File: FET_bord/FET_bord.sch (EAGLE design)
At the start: 4 parts

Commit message: スナバ回路資料追加
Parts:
- added CPOL1, CPOL2, CPOL3: C_DEKAI, user_rcl:C_DEKAI
- added R1: 0, user_rcl:R_REG
- added R_I1, R_I2: (no value), user_rcl:R_SHUGOU
- added U$1: VL_4P, user_conector:VL_4P
- added U$2: A3921, user_ic:A3921
- added U$3: ACS711, user_ic:ACS711
- added U$4: HS38382, user_heatshink:HS38382
- added U$5, U$7: FDC6305, user_tr_fet_igbt:FDC6305
- added U$6: RGB_LED, user_leds:RGB_LED
- added U$8: TLP290-4, user_ic:TLP290-4
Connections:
- new net FF1: U$5.PIN1_G1, U$7.PIN1_G1
- new net FF2: U$5.PIN3_G2, U$7.PIN3_G2
- new net GHA: U$2.PIN10_GHA
- new net GHB: U$2.PIN5_GHB
- new net GLA: U$2.PIN12_GLA
- new net GLB: U$2.PIN3_GLB
- new net GND: CPOL1.-, CPOL2.-, CPOL3.-, R1.2, TR3.PIN3_S, TR4.PIN3_S, U$1.PIN4
- new net GNDI: R1.1, U$2.PAD, U$2.PIN17_GND, U$5.PIN2_S2, U$5.PIN5_S1, U$6.B_A
- new net M: U$1.PIN3, U$3.1_IP+, U$3.2_IP+
- new net N$1: U$5.PIN6_D1, U$6.R_A
- new net N$2: TR1.PIN3_S, TR3.PIN2_D, U$3.3_IP-, U$3.4_IP-
- new net N$3: TR2.PIN3_S, TR4.PIN2_D
- new net N$4: U$1.PIN2
- new net N$5: U$5.PIN4_D2, U$6.G_A
- new net N$6: R_I1.1, U$6.R_K
- new net N$7: R_I1.2, U$6.G_K
- new net N$8: R_I1.3, U$6.B_K
- new net SA: U$2.PIN11_SA
- new net SB: U$2.PIN4_SB
- new net VDD: CPOL1.+, CPOL2.+, CPOL3.+, TR1.PIN2_D, TR2.PIN2_D, U$1.PIN1

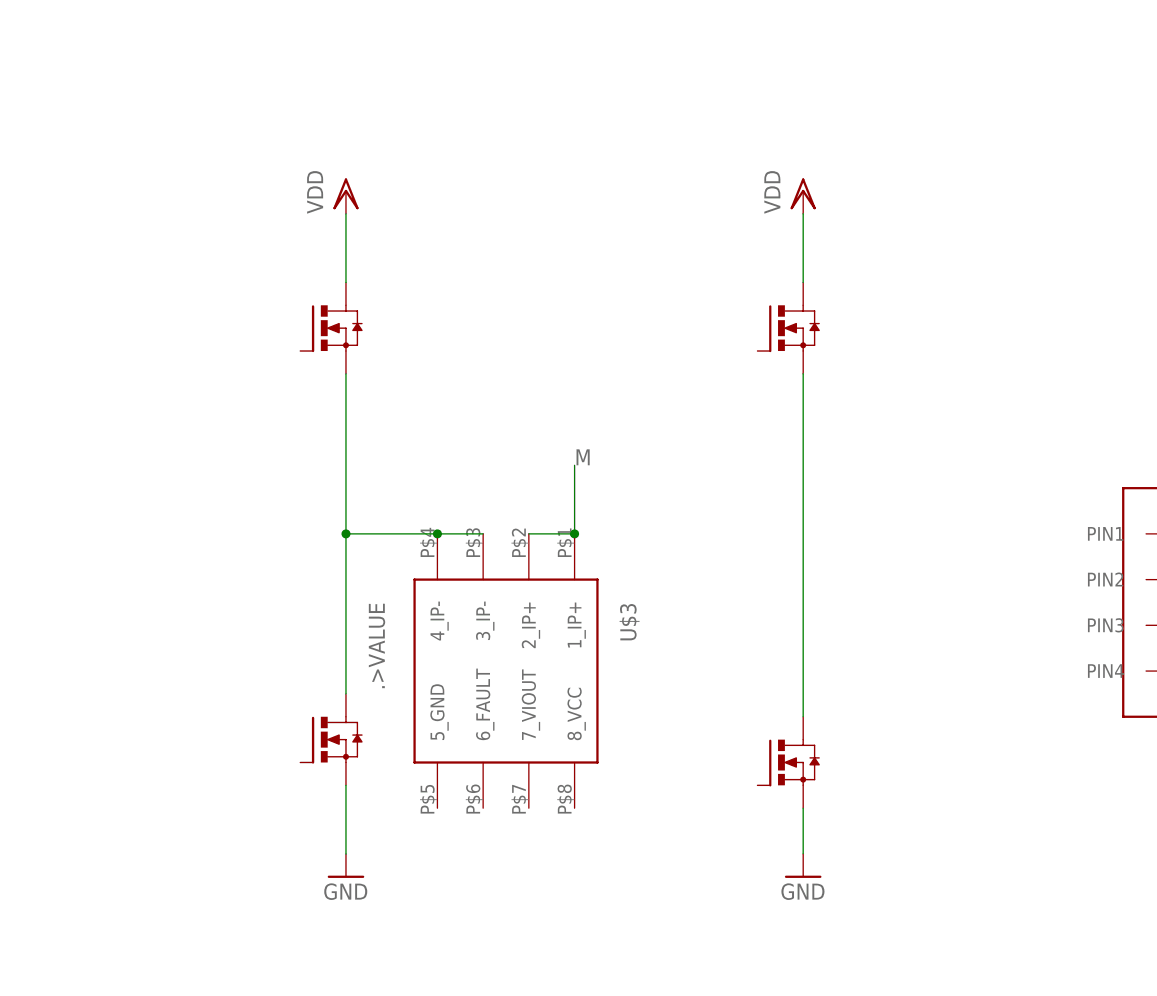
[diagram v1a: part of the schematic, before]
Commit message: スナバ追加
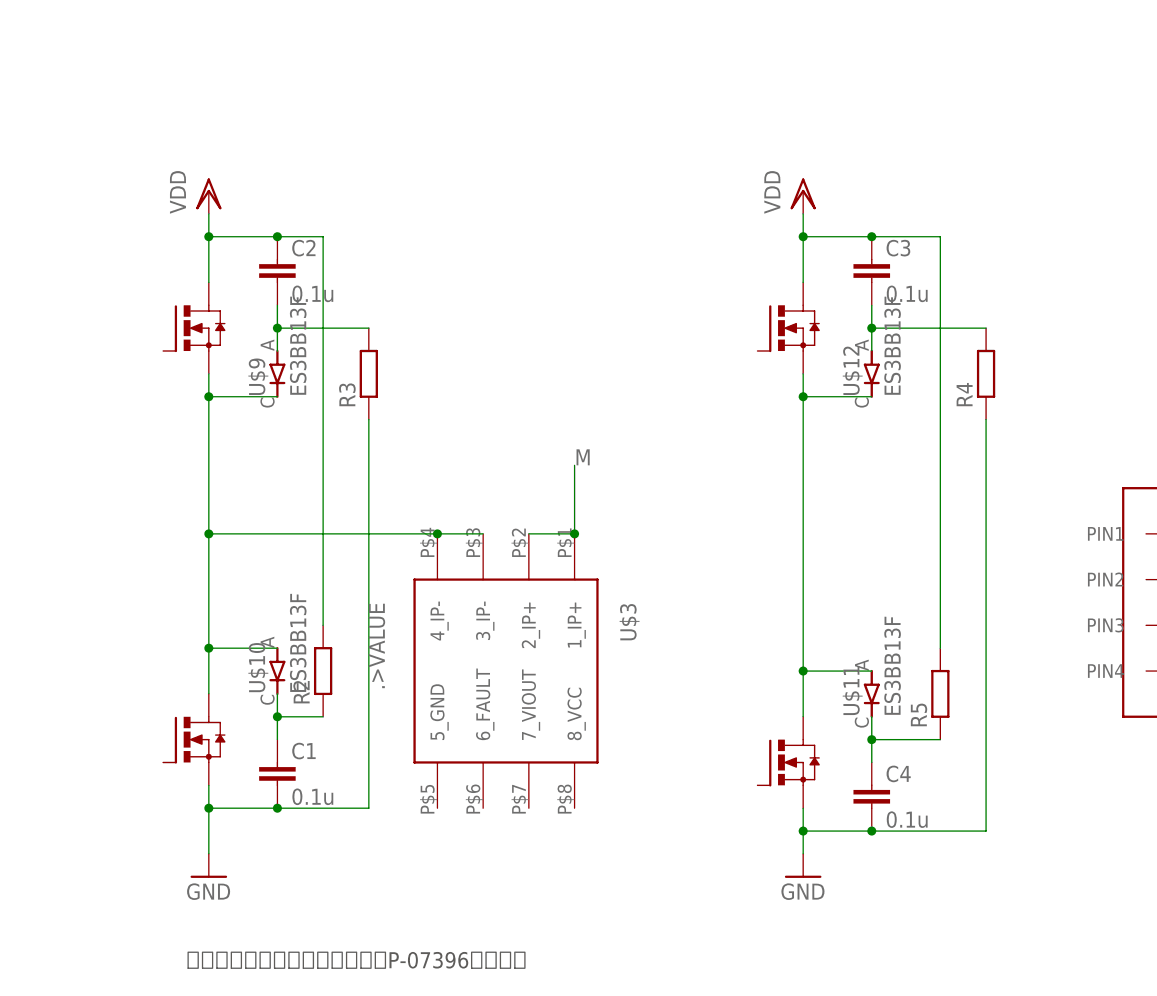
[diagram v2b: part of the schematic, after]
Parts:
- added C1, C2, C3, C4: 0.1u, rcl:C-EUC3216
- added R2, R3, R4, R5: (no value), user_rcl:R_REG1632*
- added U$10, U$11, U$12, U$9: ES3BB13F, user_diode:ES3BB13F
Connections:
- new net N$10: C2.2, R3.2, U$9.A
- new net N$11: C3.2, R4.2, U$12.A
- new net N$12: C4.1, R5.1, U$11.C
- new net N$9: C1.1, R2.1, U$10.C
- net GND: now also C1.2, C4.2, R3.1, R4.1
- net N$2: now also U$10.A, U$9.C
- net N$3: now also U$11.A, U$12.C
- net VDD: now also C2.1, C3.1, R2.2, R5.2
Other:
- note added: "スナバコンデンサは秋月電子のP-07396を用いる"

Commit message: a3921ロジック回路周りの設計
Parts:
- added C5: 0.1u, rcl:C-EUC1608
- added R6: (no value), user_rcl:R_REG
- added R7: 20k, user_rcl:R_REG
- added R_I3, R_I4: 10k, user_rcl:R_SHUGOU2
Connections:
- new net N$13: R_I3.1, U$2.PIN23_PWMH
- new net N$14: R_I3.2, U$2.PIN22_PWML
- new net N$15: R_I3.3, U$2.PIN21_SR
- new net N$16: R_I3.4, U$2.PIN19_PHASE
- new net RDEAD: U$2.PIN27_RDEAD
- new net RESET: U$2.PIN24_RESET
- new net V5: C5.1, R_I3.5, R_I3.6, R_I3.7, R_I4.5, R_I4.6, R_I4.7, U$2.PIN20_V5
- new net VDSTH: R6.1, R7.1, R_I4.1, R_I4.4, U$2.PIN28_VDSTH
- net FF1: now also R_I4.2, U$2.PIN25_FF1
- net FF2: now also R_I4.3, U$2.PIN26_FF2
- net GNDI: now also C5.2, R6.2, R7.2, R_I3.8, R_I4.8
- net VDD: now also U$2.PIN13_VBB
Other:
- note added: "deadtime = 280ns"
- moved on the sheet: R1

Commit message: ロジック部を設計
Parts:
- removed U$8: TLP290-4, user_ic:TLP290-4
- added C6: 0.1u, rcl:C-EUC1608
- added IC_1: (no value), user_ic:TLP291
- added IC_2: (no value), user_ic:TLP290-4
- added IC_3: (no value), user_ic:TLP152
- added R10, R9: 10k, user_rcl:R_REG
- added R8: 33k, user_rcl:R_REG
- added R_I5: 1k, user_rcl:R_SHUGOU
- R6: value (none) -> 2.4k
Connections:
- new net +3V3: R10.2, R9.2
- new net COAST: IC_2.2_C, R_I3.3, U$2.PIN21_SR, U$2.PIN22_PWML
- new net COAST_IN: R_I5.4
- new net DIR: IC_2.1_C, R_I3.4, U$2.PIN19_PHASE
- new net DIR_IN: R_I5.3
- new net FF1O: IC_2.3_K, R_I2.8
- new net FF1_IN: IC_2.3_C, R9.1
- new net FF2O: IC_2.4_K, R_I2.5
- new net FF2_IN: IC_2.4_C, R10.1
- new net GNDINT: IC_1.2_K, IC_2.1_K, IC_2.2_K, IC_2.3_E, IC_2.4_E, IC_3.K
- new net N$17: IC_2.1_A, R_I5.6
- new net N$18: IC_2.2_A, R_I5.5
- new net PWM: IC_3.OUT, R_I3.1, U$2.PIN23_PWMH
- new net PWM_IN: R_I5.1
- new net RESET_IN: R_I5.2
- net GNDI: now also C6.2, IC_1.3_E, IC_2.1_E, IC_2.2_E, IC_3.GND, U$7.PIN2_S2, U$7.PIN5_S1
- net N$13: now also IC_3.A, R_I5.8; no longer R_I3.1, U$2.PIN23_PWMH
- net N$14: now also R_I2.4, U$7.PIN4_D2; no longer R_I3.2, U$2.PIN22_PWML
- net N$15: now also R_I2.1, U$7.PIN6_D1; no longer R_I3.3, U$2.PIN21_SR
- net N$16: now also IC_1.1_A, R_I5.7; no longer R_I3.4, U$2.PIN19_PHASE
- net RDEAD: now also R7.1, R_I4.1
- net RESET: now also IC_1.4_C, R8.1
- net V5: now also C6.1, IC_2.3_A, IC_2.4_A, IC_3.VCC, R8.2, R_I1.6, R_I1.7, R_I1.8; no longer R_I3.7
- net VDSTH: no longer R7.1, R_I4.1
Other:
- moved on the sheet: C1, C2, C3, C4, C5, CPOL1, CPOL2, CPOL3, R1, R2, R3, R4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

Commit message: 回路図ほぼ完成
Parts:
- added C10: 10u, rcl:C-EUC1608
- added C11, C12, C13, C14: 0.1u, rcl:C-EUC1608
- added C15: 4.7u, rcl:C-EUC1608
- added C16, C19: 2.2u, rcl:C-EUC1608
- added C17: 100u, rcl:C-EUC3216
- added C18, C7: 1u, rcl:C-EUC1608
- added C8, C9: 0.22u, rcl:C-EUC1608
- added CON1, CON2: (no value), user_conector:JQ_P8P
- added IC1: (no value), user_ic:ADP151AUJZ
- added IC2: (no value), user_ic:NJW1616T
- added L1: 22u, user_rcl:L_SMD_INDUCTOR
- added R11, R12, R13, R14, R15, R16, R17, R18, R19: (no value), user_rcl:R_REG
- added R20: 3.3k, user_rcl:R_REG
- added R21: 2k, user_rcl:R_REG
- added R22: 10k, user_rcl:R_REG
- added U$13: HS38382, user_heatshink:HS38382
- added U$8: BOX10PBOX10P-L, user_conector:BOX10PBOX10P-L
- CPOL1, CPOL2, CPOL3: value C_DEKAI -> 330u
- U$4: value HS38382 -> ss2040; device user_heatshink:HS38382 -> user_diode:SMD_DAIOD
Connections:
- removed net N$3: TR2.PIN3_S, TR4.PIN2_D, U$11.A, U$12.C
- new net 12V: C19.1, IC2.5_VIN, R22.2, U$8.P$1, U$8.P$2
- new net 5V: C15.1, IC1.1_VIN, IC1.3_EN, U$8.P$10, U$8.P$9
- new net CANH: U$8.P$5
- new net CANL: U$8.P$6
- new net FAULT: CON2.PIN4, R19.1, U$3.6_FAULT
- new net N$19: C7.1, U$2.PIN16_CP1
- new net N$20: C7.2, U$2.PIN15_CP2
- new net N$21: C8.2, U$2.PIN9_CA
- new net N$22: C9.2, U$2.PIN6_CB
- new net N$23: C10.2, U$2.PIN8_VREG
- new net N$24: C18.2, IC2.3_FB, R20.1, R21.2
- new net N$25: R13.2, R17.2, TR4.PIN1_G
- new net N$26: R14.2, R18.2, TR2.PIN1_G
- new net N$27: R11.2, R15.2, TR1.PIN1_G
- new net N$28: R12.2, R16.2, TR3.PIN1_G
- new net N$31: IC2.4_SHDN, R22.1
- new net SENS_GND: C14.1, U$3.5_GND
- new net SENS_VCC: C14.2, C16.1, IC1.5_VOUT, R19.2, U$3.8_VCC
- new net VIOUT: CON2.PIN2, U$3.7_VIOUT
- net +3V3: now also C17.1, C18.1, L1.2, R20.2
- net GHA: now also R18.1
- net GHB: now also R15.1
- net GLA: now also R17.1
- net GLB: now also R16.1
- net GND: now also C11.2, C12.2, C13.2, R12.1, R13.1
- net GNDI: now also C10.1, U$2.PIN2_LSS
- net GNDINT: now also C15.2, C16.2, C17.2, C19.2, CON2.PIN1, CON2.PIN3, IC1.2_GND, IC2.2_GND, R21.1, U$4.A, U$8.P$7, U$8.P$8
- net N$2: now also IC2.6_SW, L1.1, U$4.C; no longer TR1.PIN3_S, TR3.PIN2_D, U$10.A, U$3.3_IP-, U$3.4_IP-, U$9.C
- net SA: now also C8.1, R14.1, TR2.PIN3_S, TR4.PIN2_D, U$11.A, U$12.C
- net SB: now also C9.1, R11.1, TR1.PIN3_S, TR3.PIN2_D, U$10.A, U$3.3_IP-, U$3.4_IP-, U$9.C
- net VDD: now also C11.1, C12.1, C13.1, U$2.PIN1_VDRAIN
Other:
- note added: "電解コンデンサには秋月のP-14450を用いる"
- moved on the sheet: C3, C4, CPOL1, CPOL2, CPOL3, R4, R5, U$11, U$12, U$3

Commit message: 基板設計を開始した
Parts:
- removed C1, C2, C3, C4: 0.1u, rcl:C-EUC3216
- removed R2, R3, R4, R5: (no value), user_rcl:R_REG1632*
- R11, R12, R13, R14: value (none) -> 10k
- R15, R16, R17, R18: value (none) -> 10
- U$10, U$11, U$12, U$9: value ES3BB13F -> SBR15U30SP5; device user_diode:ES3BB13F -> user_diode:SBR15U30SP5
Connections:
- removed net N$10: C2.2, R3.2, U$9.A
- removed net N$11: C3.2, R4.2, U$12.A
- removed net N$12: C4.1, R5.1, U$11.C
- removed net N$9: C1.1, R2.1, U$10.C
- net GND: now also U$10.A1, U$10.A2, U$11.A1, U$11.A2; no longer C1.2, C4.2, R3.1, R4.1
- net SA: now also U$11.K, U$12.A1, U$12.A2; no longer U$11.A, U$12.C
- net SB: now also U$10.K, U$9.A1, U$9.A2; no longer U$10.A, U$9.C
- net VDD: now also U$12.K, U$9.K; no longer C2.1, C3.1, R2.2, R5.2
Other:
- note removed: "スナバコンデンサは秋月電子のP-07396を用いる"

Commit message: スナバ消した。基盤が結構仕上がってきた
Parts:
- removed R_I5: 1k, user_rcl:R_SHUGOU
- added C1: 0.1u, rcl:C-EUC1608
- added R2, R3, R4, R5: 1k, user_rcl:R_REG
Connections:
- removed net CANH: U$8.P$5
- removed net CANL: U$8.P$6
- removed net N$14: R_I2.4, U$7.PIN4_D2
- removed net N$15: R_I2.1, U$7.PIN6_D1
- removed net N$4: U$1.PIN2
- removed net SENS_GND: C14.1, U$3.5_GND
- new net CAN_N: CON2.PIN8, U$8.P$6
- new net CAN_P: CON2.PIN7, U$8.P$5
- new net N$3: R_I2.1, U$7.PIN4_D2
- new net N$9: R_I2.4, U$7.PIN6_D1
- net +3V3: now also CON1.PIN5, CON1.PIN6
- net COAST_IN: now also CON1.PIN3, R5.1; no longer R_I5.4
- net DIR_IN: now also CON1.PIN4, R4.1; no longer R_I5.3
- net FF1: now also R_I4.3; no longer R_I4.2
- net FF1O: now also R_I2.5; no longer R_I2.8
- net FF1_IN: now also CON1.PIN2
- net FF2: now also R_I4.2; no longer R_I4.3
- net FF2O: now also R_I2.8; no longer R_I2.5
- net FF2_IN: now also CON1.PIN1
- net GND: now also U$1.PIN1, U$2.PIN2_LSS; no longer U$1.PIN4
- net GNDI: now also C1.2, U$6.B_K; no longer U$2.PIN2_LSS, U$6.B_A
- net GNDINT: now also C14.1, CON1.PIN7, CON1.PIN8, U$3.5_GND
- net M: now also U$1.PIN2, U$3.3_IP-, U$3.4_IP-; no longer U$1.PIN3, U$3.1_IP+, U$3.2_IP+
- net N$1: now also U$6.G_K; no longer U$6.R_A
- net N$13: now also R2.2; no longer R_I5.8
- net N$16: now also R3.2; no longer R_I5.7
- net N$17: now also R4.2; no longer R_I5.6
- net N$18: now also R5.2; no longer R_I5.5
- net N$5: now also U$6.R_K; no longer U$6.G_A
- net N$6: now also U$6.B_A; no longer U$6.R_K
- net N$7: now also U$6.G_A; no longer U$6.G_K
- net N$8: now also U$6.R_A; no longer U$6.B_K
- net PWM_IN: now also CON2.PIN5, R2.1; no longer R_I5.1
- net RESET_IN: now also CON2.PIN6, R3.1; no longer R_I5.2
- net SA: now also U$3.1_IP+, U$3.2_IP+
- net SB: now also U$1.PIN3; no longer U$3.3_IP-, U$3.4_IP-
- net VDD: now also C1.1, U$1.PIN4; no longer U$1.PIN1
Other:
- note added: "CAN_P = CAN_H CAN_N = CAN_L"
- moved on the sheet: R_I2

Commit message: mcu側に着手
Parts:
- removed R19: (no value), user_rcl:R_REG
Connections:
- removed net FAULT: CON2.PIN4, R19.1, U$3.6_FAULT
- net +3V3: no longer CON1.PIN5
- net 5V: now also CON1.PIN5
- net SENS_VCC: now also CON2.PIN4; no longer R19.2
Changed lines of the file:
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@@
 <part name="CON1" library="user_conector" deviceset="JQ_P8P" device=""/>
 <part name="CON2" library="user_conector" deviceset="JQ_P8P" device=""/>
-<part name="R19" library="user_rcl" deviceset="R_REG" device=""/>
 <part name="C14" library="rcl" library_urn="urn:adsk.eagle:library:334" deviceset="C-EU" device="C1608" package3d_urn="urn:adsk.eagle:package:23621/2" value="0.1u"/>
 <part name="U$8" library="user_conector" deviceset="BOX10P" device="BOX10P-L"/>
@@
 <part name="C15" library="rcl" library_urn="urn:adsk.eagle:library:334" deviceset="C-EU" device="C1608" package3d_urn="urn:adsk.eagle:package:23621/2" value="4.7u"/>
 <part name="C16" library="rcl" library_urn="urn:adsk.eagle:library:334" deviceset="C-EU" device="C1608" package3d_urn="urn:adsk.eagle:package:23621/2" value="2.2u"/>
-<part name="GND7" library="supply1" library_urn="urn:adsk.eagle:library:371" deviceset="GNDINT" device=""/>
 <part name="GND8" library="supply1" library_urn="urn:adsk.eagle:library:371" deviceset="GNDINT" device=""/>
 <part name="GND9" library="supply1" library_urn="urn:adsk.eagle:library:371" deviceset="GNDINT" device=""/>
@@
 <part name="GND12" library="supply1" library_urn="urn:adsk.eagle:library:371" deviceset="GNDINT" device=""/>
 <part name="GND13" library="supply1" library_urn="urn:adsk.eagle:library:371" deviceset="GND" device=""/>
+<part name="GND7" library="supply1" library_urn="urn:adsk.eagle:library:371" deviceset="GNDINT" device=""/>
 </parts>
 <sheets>
@@
 <instance part="CON1" gate="G$1" x="-261.62" y="15.24" smashed="yes"/>
 <instance part="CON2" gate="G$1" x="-261.62" y="48.26" smashed="yes"/>
-<instance part="R19" gate="G$1" x="157.48" y="20.32" smashed="yes">
-<attribute name="NAME" x="153.67" y="21.8186" size="1.778" layer="95"/>
-<attribute name="VALUE" x="153.67" y="17.018" size="1.778" layer="96"/>
-</instance>
 <instance part="C14" gate="G$1" x="149.86" y="27.94" smashed="yes" rot="R90">
 <attribute name="NAME" x="149.479" y="29.464" size="1.778" layer="95" rot="R90"/>
@@
 <attribute name="VALUE" x="-128.016" y="124.841" size="1.778" layer="96"/>
 </instance>
-<instance part="GND7" gate="G$1" x="-292.1" y="53.34" smashed="yes">
-<attribute name="VALUE" x="-294.64" y="50.8" size="1.778" layer="96"/>
-</instance>
 <instance part="GND8" gate="G$1" x="-147.32" y="114.3" smashed="yes">
 <attribute name="VALUE" x="-149.86" y="111.76" size="1.778" layer="96"/>
@@
 <instance part="U$11" gate="G$1" x="203.2" y="15.24" smashed="yes" rot="R90"/>
 <instance part="U$12" gate="G$1" x="203.2" y="63.5" smashed="yes" rot="R90"/>
-<instance part="+3V3" gate="G$1" x="-259.08" y="27.94" smashed="yes"/>
+<instance part="+3V3" gate="G$1" x="-254" y="27.94" smashed="yes"/>
 <instance part="GND11" gate="G$1" x="-243.84" y="22.86" smashed="yes">
 <attribute name="VALUE" x="-246.38" y="20.32" size="1.778" layer="96"/>
@@
 <instance part="GND13" gate="1" x="-58.42" y="48.26" smashed="yes">
 <attribute name="VALUE" x="-60.96" y="45.72" size="1.778" layer="96"/>
+</instance>
+<instance part="GND7" gate="G$1" x="-292.1" y="48.26" smashed="yes">
+<attribute name="VALUE" x="-294.64" y="45.72" size="1.778" layer="96"/>
 </instance>
 </instances>
@@
 </segment>
 <segment>
-<pinref part="GND7" gate="G$1" pin="GNDINT"/>
-<wire x1="-292.1" y1="55.88" x2="-279.4" y2="55.88" width="0.1524" layer="91"/>
-<pinref part="CON2" gate="G$1" pin="PIN1"/>
-<wire x1="-279.4" y1="55.88" x2="-279.4" y2="53.34" width="0.1524" layer="91"/>
-<wire x1="-279.4" y1="55.88" x2="-269.24" y2="55.88" width="0.1524" layer="91"/>
-<junction x="-279.4" y="55.88"/>
-<pinref part="CON2" gate="G$1" pin="PIN3"/>
-<wire x1="-269.24" y1="55.88" x2="-269.24" y2="53.34" width="0.1524" layer="91"/>
-</segment>
-<segment>
 <pinref part="U$8" gate="G$1" pin="P$7"/>
 <wire x1="-256.54" y1="99.06" x2="-256.54" y2="104.14" width="0.1524" layer="91"/>
@@
 <junction x="147.32" y="27.94"/>
 </segment>
+<segment>
+<pinref part="GND7" gate="G$1" pin="GNDINT"/>
+<wire x1="-292.1" y1="50.8" x2="-292.1" y2="60.96" width="0.1524" layer="91"/>
+<pinref part="CON2" gate="G$1" pin="PIN1"/>
+<wire x1="-279.4" y1="53.34" x2="-279.4" y2="55.88" width="0.1524" layer="91"/>
+<wire x1="-279.4" y1="55.88" x2="-279.4" y2="60.96" width="0.1524" layer="91"/>
+<wire x1="-292.1" y1="60.96" x2="-279.4" y2="60.96" width="0.1524" layer="91"/>
+<pinref part="CON2" gate="G$1" pin="PIN3"/>
+<wire x1="-269.24" y1="53.34" x2="-269.24" y2="55.88" width="0.1524" layer="91"/>
+<wire x1="-279.4" y1="55.88" x2="-269.24" y2="55.88" width="0.1524" layer="91"/>
+<junction x="-279.4" y="55.88"/>
+</segment>
 </net>
 <net name="FF2_IN" class="0">
@@
 </segment>
 <segment>
-<pinref part="CON1" gate="G$1" pin="PIN5"/>
 <pinref part="CON1" gate="G$1" pin="PIN6"/>
-<wire x1="-259.08" y1="20.32" x2="-254" y2="20.32" width="0.1524" layer="91"/>
-<wire x1="-259.08" y1="20.32" x2="-259.08" y2="25.4" width="0.1524" layer="91"/>
-<junction x="-259.08" y="20.32"/>
-<label x="-259.08" y="25.4" size="1.778" layer="95" rot="R90"/>
+<label x="-254" y="27.94" size="1.778" layer="95" rot="R90"/>
 <pinref part="+3V3" gate="G$1" pin="+3V3"/>
+<wire x1="-254" y1="25.4" x2="-254" y2="20.32" width="0.1524" layer="91"/>
 </segment>
 </net>
@@
 </segment>
 </net>
-<net name="FAULT" class="0">
-<segment>
-<pinref part="U$3" gate="G$1" pin="6_FAULT"/>
-<wire x1="152.4" y1="33.02" x2="152.4" y2="20.32" width="0.1524" layer="91"/>
-<pinref part="R19" gate="G$1" pin="1"/>
-<wire x1="152.4" y1="20.32" x2="152.4" y2="17.78" width="0.1524" layer="91"/>
-<junction x="152.4" y="20.32"/>
-<label x="152.4" y="17.78" size="1.778" layer="95" rot="R270"/>
-</segment>
-<segment>
-<pinref part="CON2" gate="G$1" pin="PIN4"/>
-<wire x1="-264.16" y1="53.34" x2="-264.16" y2="60.96" width="0.1524" layer="91"/>
-<label x="-264.16" y="60.96" size="1.778" layer="95" rot="R90"/>
-</segment>
-</net>
 <net name="VIOUT" class="0">
 <segment>
@@
 <pinref part="U$3" gate="G$1" pin="8_VCC"/>
 <wire x1="162.56" y1="33.02" x2="162.56" y2="27.94" width="0.1524" layer="91"/>
-<pinref part="R19" gate="G$1" pin="2"/>
-<wire x1="162.56" y1="27.94" x2="162.56" y2="20.32" width="0.1524" layer="91"/>
-<wire x1="162.56" y1="20.32" x2="162.56" y2="17.78" width="0.1524" layer="91"/>
-<junction x="162.56" y="20.32"/>
+<wire x1="162.56" y1="27.94" x2="162.56" y2="17.78" width="0.1524" layer="91"/>
 <label x="162.56" y="17.78" size="1.778" layer="95" rot="R270"/>
 <pinref part="C14" gate="G$1" pin="2"/>
@@
 <label x="-116.84" y="132.08" size="1.778" layer="95"/>
 <label x="-116.84" y="132.08" size="1.778" layer="95"/>
+</segment>
+<segment>
+<pinref part="CON2" gate="G$1" pin="PIN4"/>
+<wire x1="-264.16" y1="53.34" x2="-264.16" y2="60.96" width="0.1524" layer="91"/>
+<label x="-264.16" y="60.96" size="1.778" layer="95" rot="R90"/>
 </segment>
 </net>
@@
 <label x="-180.34" y="132.08" size="1.778" layer="95" rot="R180"/>
 </segment>
-</net>
+<segment>
+<pinref part="CON1" gate="G$1" pin="PIN5"/>
+<wire x1="-259.08" y1="20.32" x2="-259.08" y2="25.4" width="0.1524" layer="91"/>
+<label x="-259.08" y="25.4" size="1.778" layer="95" rot="R90"/>
+</segment>
+</net>
